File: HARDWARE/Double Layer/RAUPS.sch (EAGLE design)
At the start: 52 parts, among them Q2 STP55NF06L, Q3 STP55NF06L, U1 ARDUINOR3-BPLACE

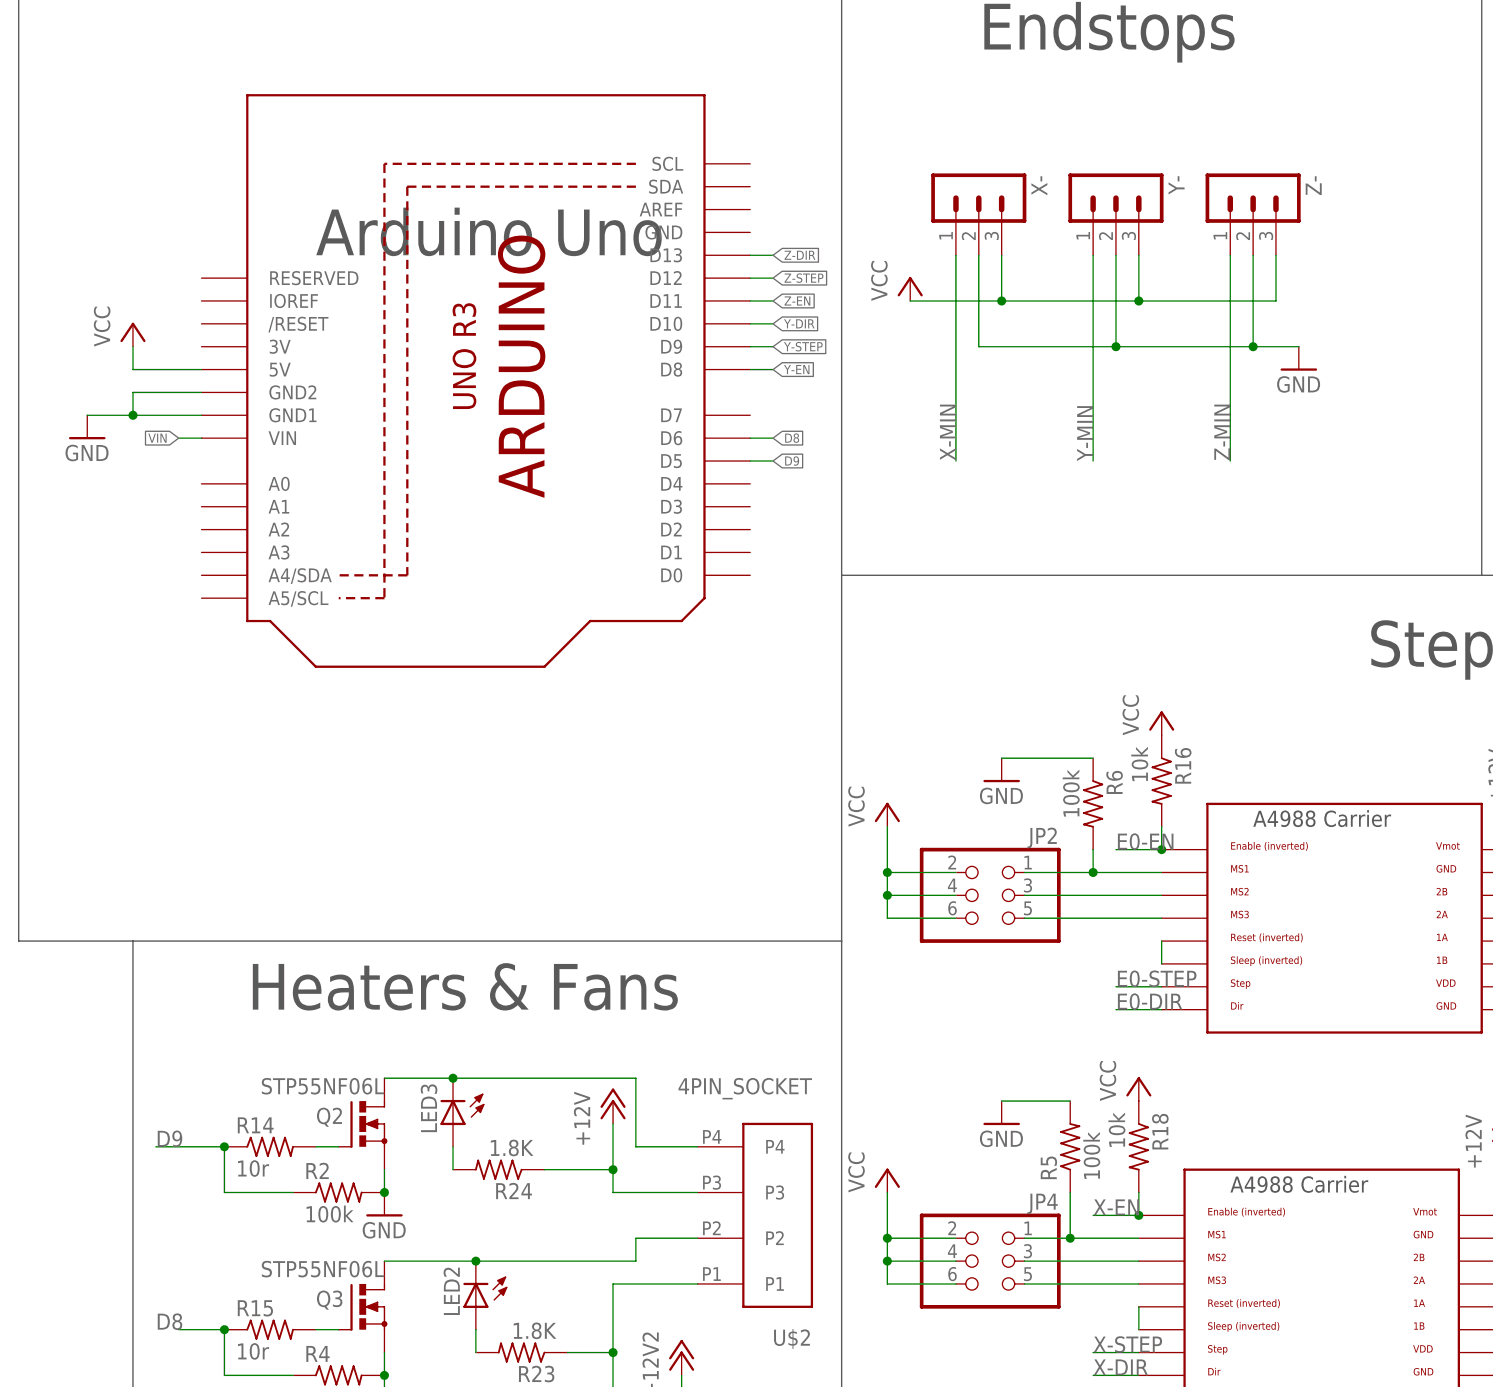
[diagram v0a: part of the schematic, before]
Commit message: Finished routing of 2 layer board, DRC complete
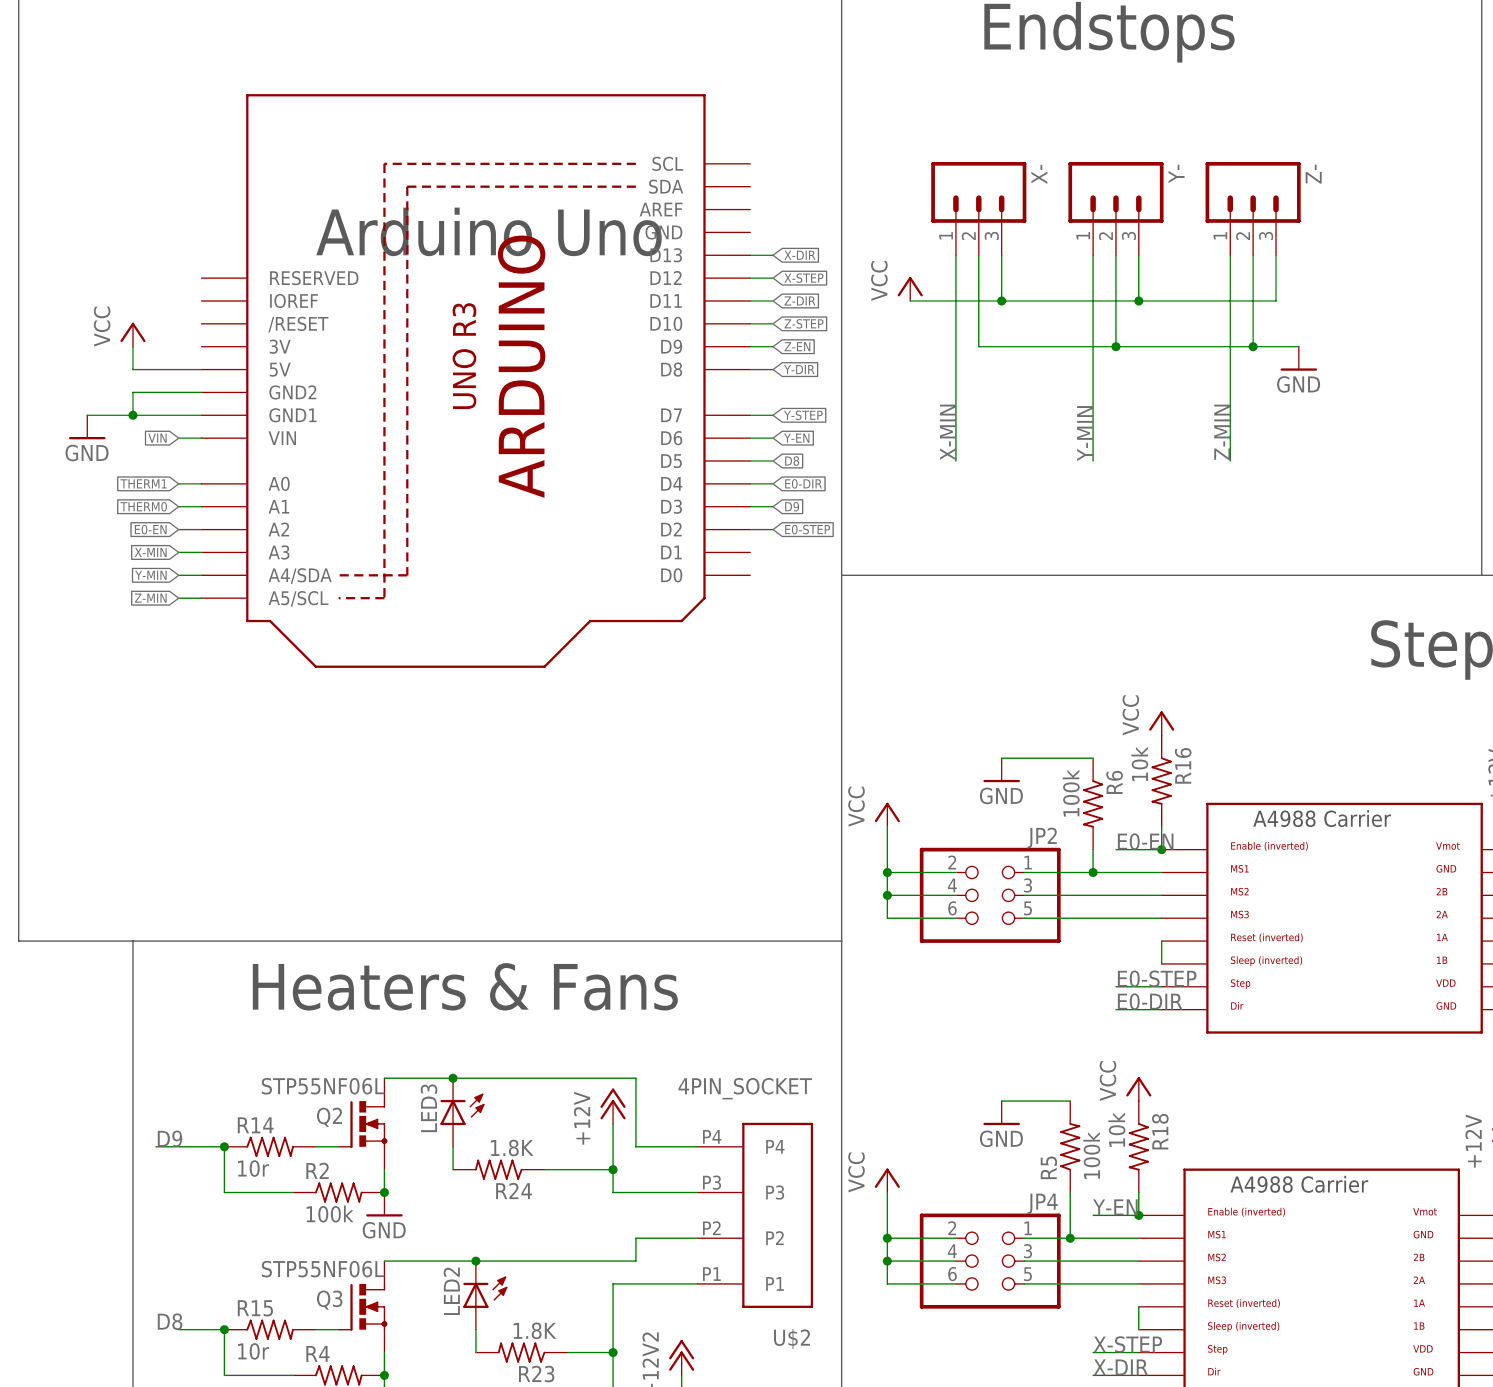
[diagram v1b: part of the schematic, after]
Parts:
- E0-DRIVE, Y-DRIVE, Z-DRIVE: value A4988BREAKOUT -> POLOLU_A4983CARRIER; device RepRapjr:A4988BREAKOUT -> RepRapjr:POLOLU_A4983CARRIER
- X-, Y-, Z-: device ultimachine:3PIN-HEADER -> SparkFun-Connectors:M03PTH
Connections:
- removed net X-EN: R18.2, X-DRIVE.EN
- net D8: now also U1.D5; no longer U1.D6
- net D9: now also U1.D3; no longer U1.D5
- net E0-DIR: now also U1.D4
- net E0-EN: now also U1.A2
- net E0-STEP: now also U1.D2
- net THERM0: now also U1.A1
- net THERM1: now also U1.A0
- net X-DIR: now also U1.D13
- net X-MIN: now also U1.A3
- net X-STEP: now also U1.D12
- net Y-DIR: now also U1.D8; no longer U1.D10
- net Y-EN: now also R18.2, U1.D6, X-DRIVE.EN; no longer U1.D8
- net Y-MIN: now also U1.A4/SDA
- net Y-STEP: now also U1.D7; no longer U1.D9
- net Z-DIR: now also U1.D11; no longer U1.D13
- net Z-EN: now also U1.D9; no longer U1.D11
- net Z-MIN: now also U1.A5/SCL
- net Z-STEP: now also U1.D10; no longer U1.D12
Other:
- moved on the sheet: X-, Y-, Z-
